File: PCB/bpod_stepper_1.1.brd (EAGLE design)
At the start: 83.8 x 63.5 mm, 30 parts, among them IC1 LM3480-5.0, IC2 SN65HVD31DR, J1 282841-4, J8 POWER_JACK

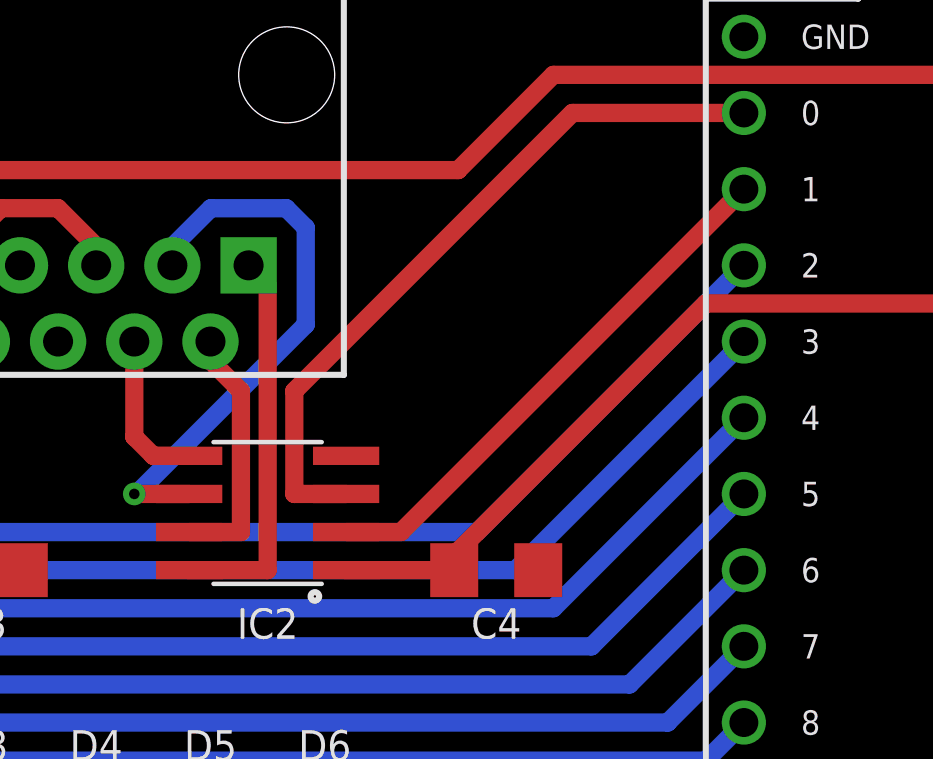
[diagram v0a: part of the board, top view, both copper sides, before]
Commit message: corrected wrong routing for RX & TX
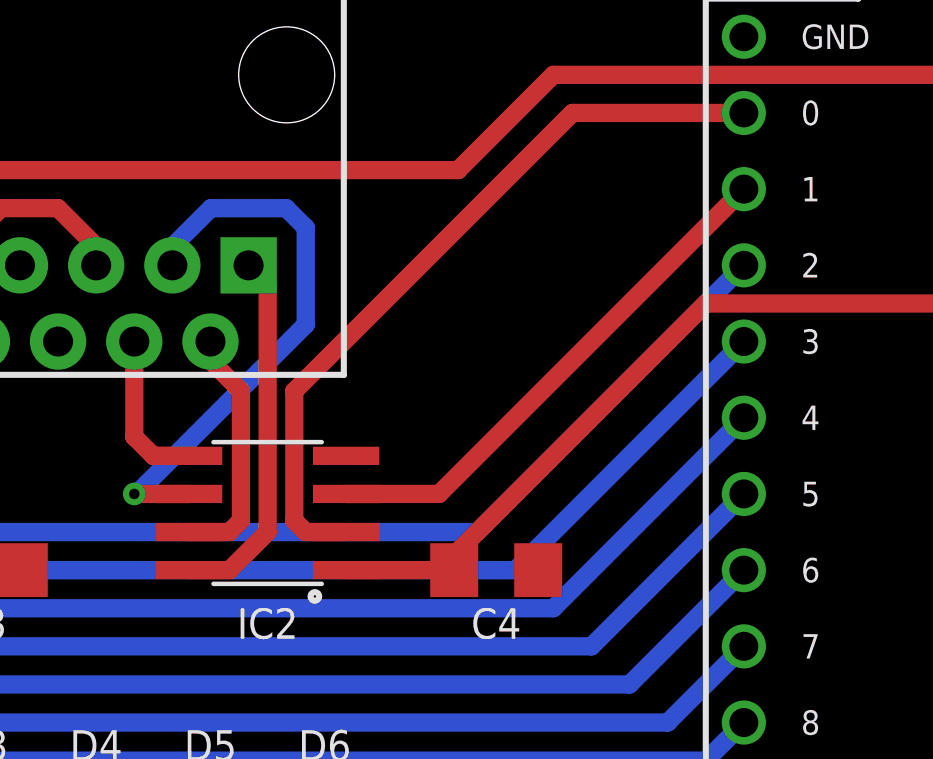
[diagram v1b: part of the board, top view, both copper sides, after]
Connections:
- net RX1: now also IC2.2; no longer IC2.3
- net TX1: now also IC2.3; no longer IC2.2
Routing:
- net RX1: track 24.0 -> 25.0 mm
- net N$7: track 13.0 -> 12.3 mm
- net TX1: track 18.0 -> 17.5 mm
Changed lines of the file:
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@@
 <layer number="14" name="Route14" color="22" fill="1" visible="no" active="no"/>
 <layer number="15" name="Route15" color="23" fill="1" visible="no" active="no"/>
-<layer number="16" name="Bottom" color="1" fill="1" visible="yes" active="yes"/>
+<layer number="16" name="Bottom" color="1" fill="1" visible="no" active="yes"/>
 <layer number="17" name="Pads" color="2" fill="1" visible="yes" active="yes"/>
 <layer number="18" name="Vias" color="2" fill="1" visible="yes" active="yes"/>
@@
 <signal name="TX1">
 <contactref element="U$1" pad="1"/>
-<contactref element="IC2" pad="2"/>
-<wire x1="46.355" y1="44.45" x2="57.785" y2="55.88" width="0.6096" layer="1"/>
-<wire x1="44.5262" y1="44.45" x2="46.355" y2="44.45" width="0.6096" layer="1"/>
+<contactref element="IC2" pad="3"/>
+<wire x1="47.625" y1="45.72" x2="57.785" y2="55.88" width="0.6096" layer="1"/>
+<wire x1="44.5262" y1="45.72" x2="47.625" y2="45.72" width="0.6096" layer="1"/>
 </signal>
 <signal name="RX1">
@@
 <wire x1="52.07" y1="58.42" x2="42.799" y2="49.149" width="0.6096" layer="1"/>
 <contactref element="U$1" pad="0"/>
-<contactref element="IC2" pad="3"/>
-<wire x1="42.799" y1="49.149" x2="42.799" y2="45.72" width="0.6096" layer="1"/>
-<wire x1="42.799" y1="45.72" x2="44.5262" y2="45.72" width="0.6096" layer="1"/>
+<contactref element="IC2" pad="2"/>
+<wire x1="42.799" y1="49.149" x2="42.799" y2="44.831" width="0.6096" layer="1"/>
+<wire x1="42.799" y1="44.831" x2="43.18" y2="44.45" width="0.6096" layer="1"/>
+<wire x1="43.18" y1="44.45" x2="44.5262" y2="44.45" width="0.6096" layer="1"/>
 </signal>
 <signal name="N$7">
 <contactref element="IC2" pad="8"/>
 <contactref element="U$2" pad="1"/>
-<wire x1="39.2938" y1="43.18" x2="41.91" y2="43.18" width="0.6096" layer="1"/>
-<wire x1="41.91" y1="43.18" x2="41.91" y2="52.705" width="0.6096" layer="1"/>
+<wire x1="39.2938" y1="43.18" x2="40.64" y2="43.18" width="0.6096" layer="1"/>
+<wire x1="40.64" y1="43.18" x2="41.91" y2="44.45" width="0.6096" layer="1"/>
+<wire x1="41.91" y1="44.45" x2="41.91" y2="52.705" width="0.6096" layer="1"/>
 <wire x1="41.91" y1="52.705" x2="41.275" y2="53.34" width="0.6096" layer="1"/>
 </signal>
@@
 <contactref element="U$2" pad="2"/>
 <contactref element="IC2" pad="7"/>
-<wire x1="39.2938" y1="44.45" x2="41.021" y2="44.45" width="0.6096" layer="1"/>
-<wire x1="41.021" y1="44.45" x2="41.021" y2="49.149" width="0.6096" layer="1"/>
+<wire x1="39.2938" y1="44.45" x2="40.64" y2="44.45" width="0.6096" layer="1"/>
+<wire x1="40.64" y1="44.45" x2="41.021" y2="44.831" width="0.6096" layer="1"/>
+<wire x1="41.021" y1="44.831" x2="41.021" y2="49.149" width="0.6096" layer="1"/>
 <wire x1="41.021" y1="49.149" x2="40.005" y2="50.165" width="0.6096" layer="1"/>
 <wire x1="40.005" y1="50.165" x2="40.005" y2="50.8" width="0.6096" layer="1"/>
